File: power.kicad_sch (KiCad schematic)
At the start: 45 parts, among them U2 TPS56A37, U6 TPS5430DDA, U7 TPS56A37

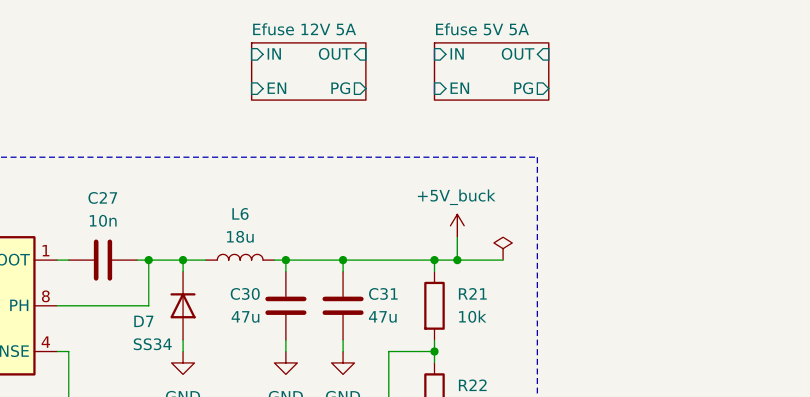
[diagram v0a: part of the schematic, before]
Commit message: schem: add ILM pins and 12V 10A rail
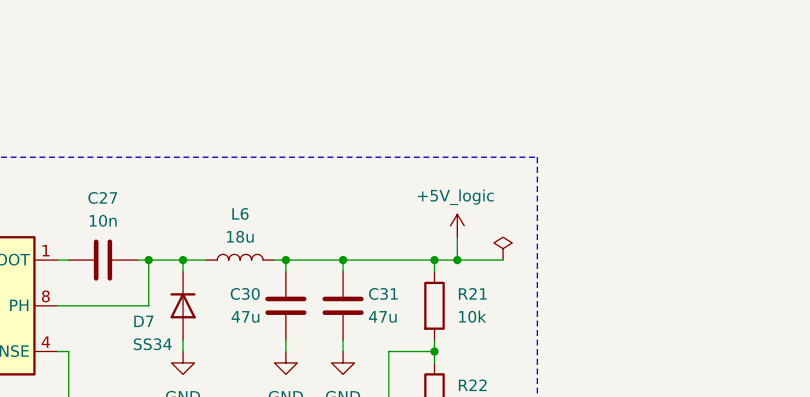
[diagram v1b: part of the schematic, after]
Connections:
- net +5V_buck renamed +5V_logic
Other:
- removed sheet Efuse 12V 5A
- removed sheet Efuse 5V 5A
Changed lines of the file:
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@@
 			)
 		)
-		(property "Value" "+5V_buck"
+		(property "Value" "+5V_logic"
 			(at 144.018 33.528 0)
 			(effects
@@
 				)
 			)
-		)
-	)
-	(sheet
-		(at 125.73 16.51)
-		(size 12.7 6.35)
-		(exclude_from_sim no)
-		(in_bom yes)
-		(on_board yes)
-		(dnp no)
-		(fields_autoplaced yes)
-		(stroke
-			(width 0.1524)
-			(type solid)
-		)
-		(fill
-			(color 0 0 0 0.0000)
-		)
-		(property "Sheetname" "Efuse 12V 5A"
-			(at 125.73 15.7984 0)
-			(effects
-				(font
-					(size 1.27 1.27)
-				)
-				(justify left bottom)
-			)
-		)
-		(property "Sheetfile" "efuse-12-5.kicad_sch"
-			(at 125.73 23.4446 0)
-			(effects
-				(font
-					(size 1.27 1.27)
-				)
-				(justify left top)
-				(hide yes)
-			)
-		)
-		(pin "EN" input
-			(at 125.73 21.59 180)
-			(effects
-				(font
-					(size 1.27 1.27)
-				)
-				(justify left)
-			)
-		)
-		(pin "PG" output
-			(at 138.43 21.59 0)
-			(effects
-				(font
-					(size 1.27 1.27)
-				)
-				(justify right)
-			)
-		)
-		(pin "OUT" input
-			(at 138.43 17.78 0)
-			(effects
-				(font
-					(size 1.27 1.27)
-				)
-				(justify right)
-			)
-		)
-		(pin "IN" input
-			(at 125.73 17.78 180)
-			(effects
-				(font
-					(size 1.27 1.27)
-				)
-				(justify left)
-			)
-		)
-		(instances
-			(project "valrob-carte-alim-cdf-1"
-				(path "/8d7b287d-627f-46aa-8c27-0b5ed29ab4a2/0cc01053-a223-4e8e-b0aa-a1ec618db290"
-					(page "3")
-				)
-			)
-		)
-	)
-	(sheet
-		(at 146.05 16.51)
-		(size 12.7 6.35)
-		(exclude_from_sim no)
-		(in_bom yes)
-		(on_board yes)
-		(dnp no)
-		(fields_autoplaced yes)
-		(stroke
-			(width 0.1524)
-			(type solid)
-		)
-		(fill
-			(color 0 0 0 0.0000)
-		)
-		(property "Sheetname" "Efuse 5V 5A"
-			(at 146.05 15.7984 0)
-			(effects
-				(font
-					(size 1.27 1.27)
-				)
-				(justify left bottom)
-			)
-		)
-		(property "Sheetfile" "efuse-5-5.kicad_sch"
-			(at 146.05 23.4446 0)
-			(effects
-				(font
-					(size 1.27 1.27)
-				)
-				(justify left top)
-				(hide yes)
-			)
-		)
-		(pin "EN" input
-			(at 146.05 21.59 180)
-			(effects
-				(font
-					(size 1.27 1.27)
-				)
-				(justify left)
-			)
-		)
-		(pin "PG" output
-			(at 158.75 21.59 0)
-			(effects
-				(font
-					(size 1.27 1.27)
-				)
-				(justify right)
-			)
-		)
-		(pin "OUT" input
-			(at 158.75 17.78 0)
-			(effects
-				(font
-					(size 1.27 1.27)
-				)
-				(justify right)
-			)
-		)
-		(pin "IN" input
-			(at 146.05 17.78 180)
-			(effects
-				(font
-					(size 1.27 1.27)
-				)
-				(justify left)
-			)
-		)
-		(instances
-			(project "valrob-carte-alim-cdf-1"
-				(path "/8d7b287d-627f-46aa-8c27-0b5ed29ab4a2/0cc01053-a223-4e8e-b0aa-a1ec618db290"
-					(page "4")
-				)
-			)

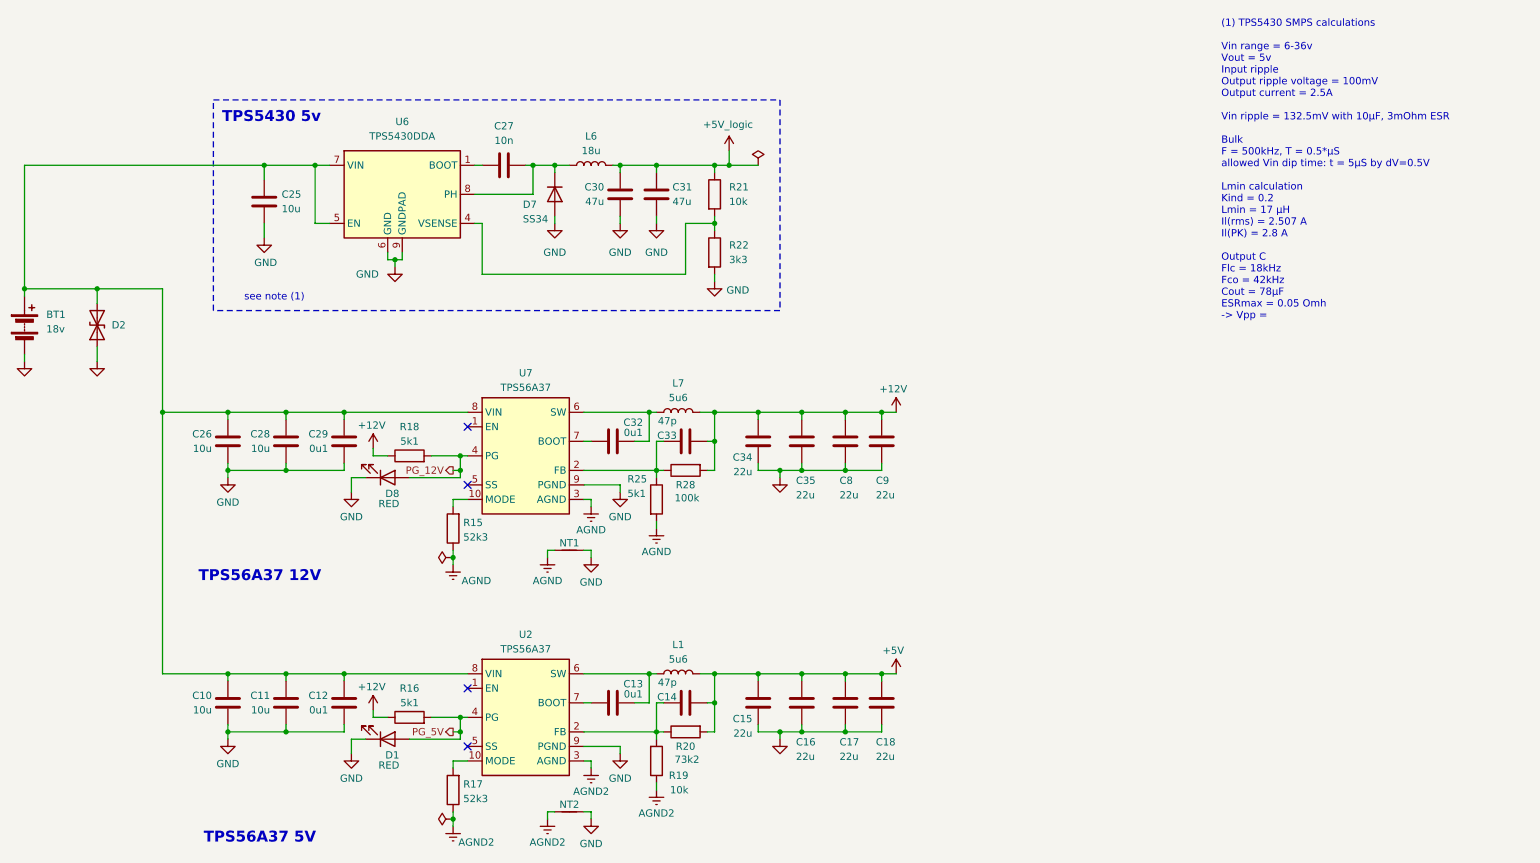
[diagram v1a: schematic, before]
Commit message: schem: reorganize connectors
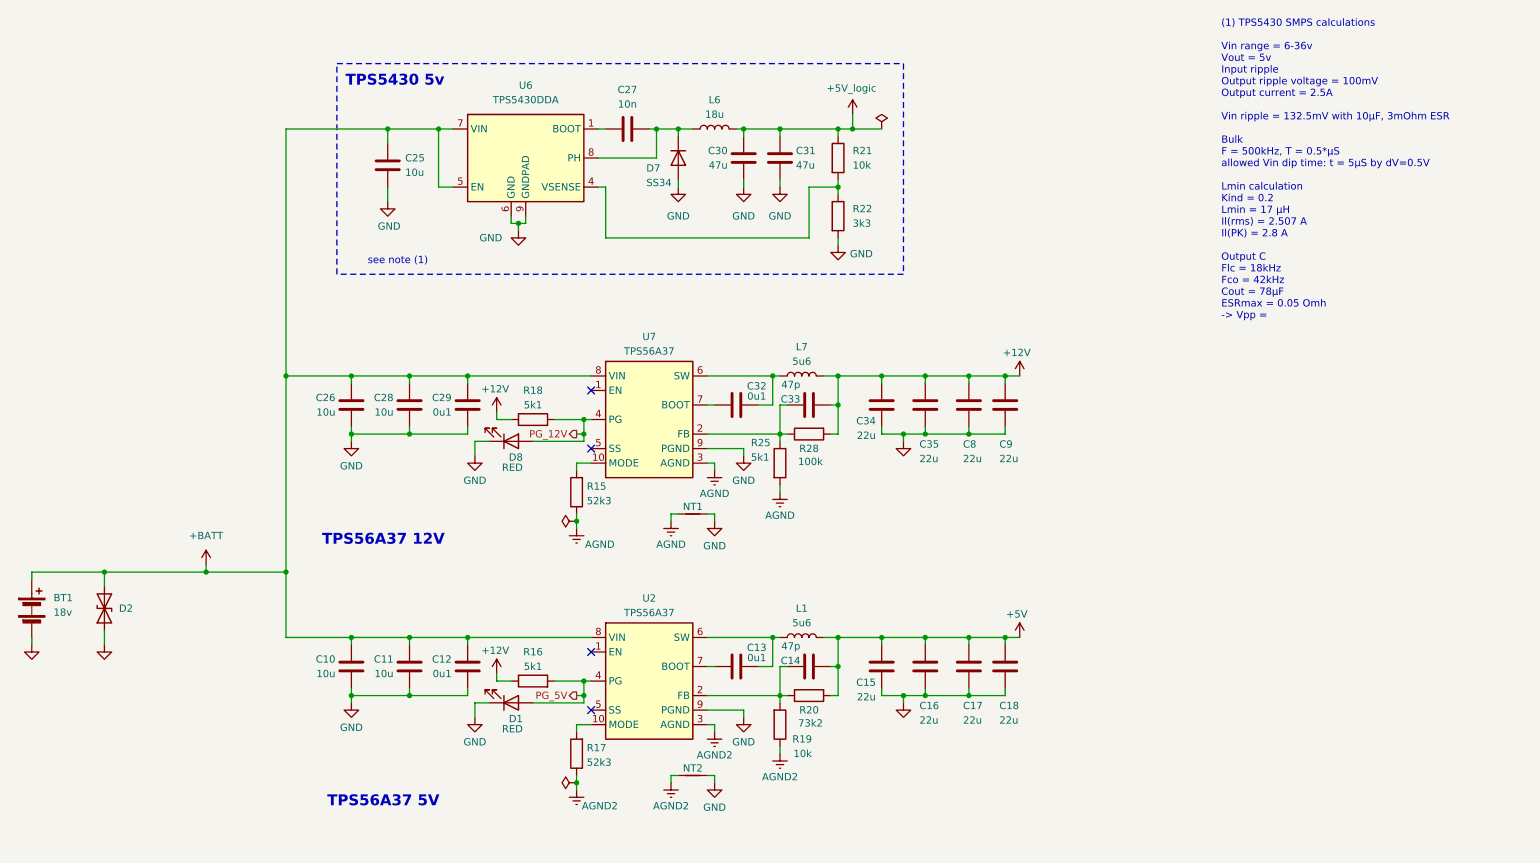
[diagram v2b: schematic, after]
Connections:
- net +BATT: now reaches BT1.1 (+), C10.1, C11.1, C12.1, C25.1, C26.1, C28.1, C29.1, D2.2 (A2), U2.8 (VIN), U6.5 (EN), U6.7 (VIN), U7.8 (VIN)
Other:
- moved on the sheet: BT1, C10, C11, C12, C13, C14, C15, C16, C17, C18, C25, C26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

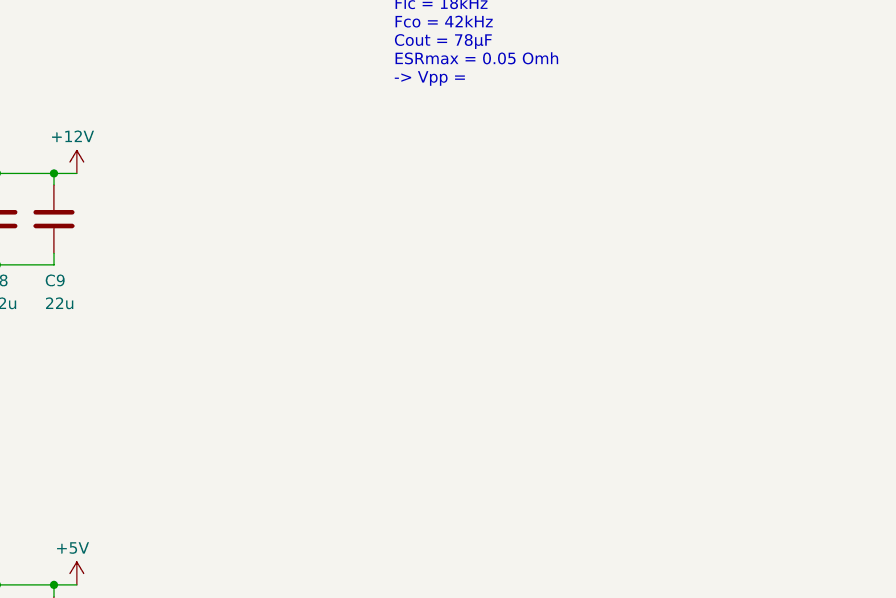
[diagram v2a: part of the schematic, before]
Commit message: schem: add CAN transceiver
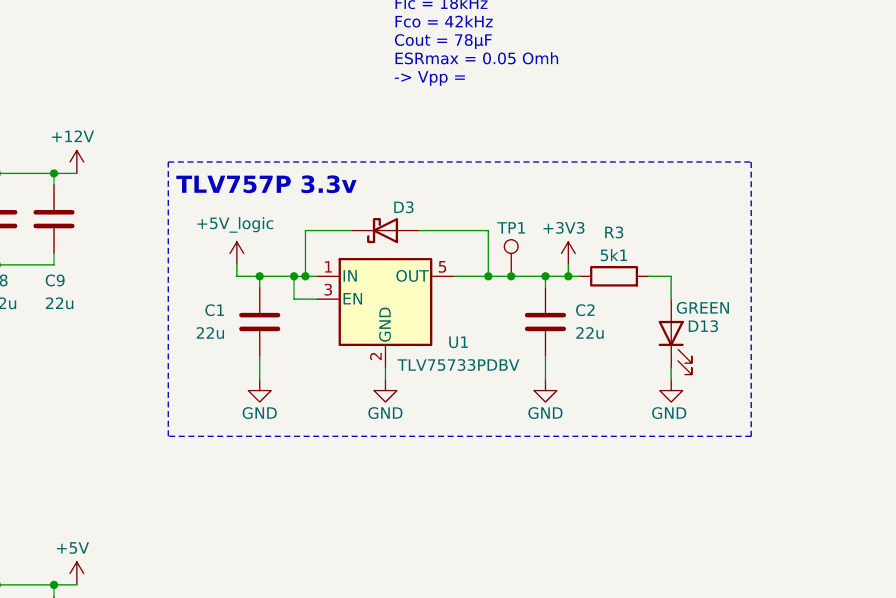
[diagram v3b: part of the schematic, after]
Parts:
- added C1, C2: 22u, Capacitor_SMD:C_0603_1608Metric, symbol Device:C
- added D13: GREEN, LED_SMD:LED_0805_2012Metric, symbol Device:LED
- added D3: D_Schottky, Diode_SMD:D_SMA, symbol Device:D_Schottky
- added R3: 5k1, Resistor_SMD:R_0402_1005Metric, symbol Device:R
- added TP1: TestPoint, TestPoint:TestPoint_Pad_D2.0mm, symbol Connector:TestPoint
- added U1: TLV75733PDBV, Package_TO_SOT_SMD:SOT-23-5, symbol Regulator_Linear:TLV75733PDBV
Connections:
- net +5V_logic: now also C1.2, D3.1 (K), U1.1 (IN), U1.3 (EN)
- net GND: now also C1.1, C2.1, D13.1 (K), U1.2 (GND)
- new net: D13.2 (A), R3.2
- new net +3V3: C2.2, D3.2 (A), R3.1, TP1.1, U1.5 (OUT)
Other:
- note added: "TLV757P 3.3v"

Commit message: schem: add additional connector for batt vin
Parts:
- added J25: Conn_01x02, Connector_JST:JST_XH_B2B-XH-A_1x02_P2.50mm_Vertical, symbol Connector_Generic:Conn_01x02
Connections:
- net +BATT: now also J25.2 (Pin_2)
- net GND: now also J25.1 (Pin_1)
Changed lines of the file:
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@@
 	)
 	(junction
+		(at 48.26 111.76)
+		(diameter 0)
+		(color 0 0 0 0)
+	)
+	(junction
 		(at 123.19 87.63)
 		(diameter 0)
@@
 	(wire
 		(pts
+			(xy 48.26 121.92) (xy 50.8 121.92)
+		)
+		(stroke
+			(width 0)
+			(type default)
+		)
+	)
+	(wire
+		(pts
 			(xy 127 53.34) (xy 127 44.45)
 		)
@@
 	(wire
 		(pts
-			(xy 39.37 111.76) (xy 57.15 111.76)
+			(xy 39.37 111.76) (xy 48.26 111.76)
 		)
 		(stroke
@@
 	(wire
 		(pts
+			(xy 48.26 119.38) (xy 48.26 111.76)
+		)
+		(stroke
+			(width 0)
+			(type default)
+		)
+	)
+	(wire
+		(pts
 			(xy 102.87 77.47) (xy 124.46 77.47)
 		)
@@
 	(wire
 		(pts
+			(xy 48.26 121.92) (xy 48.26 125.73)
+		)
+		(stroke
+			(width 0)
+			(type default)
+		)
+	)
+	(wire
+		(pts
 			(xy 190.5 133.35) (xy 196.85 133.35)
 		)
@@
 	(wire
 		(pts
+			(xy 50.8 119.38) (xy 48.26 119.38)
+		)
+		(stroke
+			(width 0)
+			(type default)
+		)
+	)
+	(wire
+		(pts
 			(xy 251.46 88.9) (xy 251.46 90.17)
 		)
@@
 	(wire
 		(pts
+			(xy 48.26 111.76) (xy 57.15 111.76)
+		)
+		(stroke
+			(width 0)
+			(type default)
+		)
+	)
+	(wire
+		(pts
 			(xy 151.13 90.17) (xy 144.78 90.17)
 		)
@@
 	)
 	(symbol
+		(lib_id "Connector_Generic:Conn_01x02")
+		(at 55.88 121.92 0)
+		(mirror x)
+		(unit 1)
+		(exclude_from_sim no)
+		(in_bom yes)
+		(on_board yes)
+		(dnp no)
+		(fields_autoplaced yes)
+		(property "Reference" "J25"
+			(at 55.88 115.57 0)
+			(effects
+				(font
+					(size 1.27 1.27)
+				)
+			)
+		)
+		(property "Value" "Conn_01x02"
+			(at 58.42 119.3801 0)
+			(effects
+				(font
+					(size 1.27 1.27)
+				)
+				(justify left)
+				(hide yes)
+			)
+		)
+		(property "Footprint" "Connector_JST:JST_XH_B2B-XH-A_1x02_P2.50mm_Vertical"
+			(at 55.88 121.92 0)
+			(effects
+				(font
+					(size 1.27 1.27)
+				)
+				(hide yes)
+			)
+		)
+		(property "Datasheet" "~"
+			(at 55.88 121.92 0)
+			(effects
+				(font
+					(size 1.27 1.27)
+				)
+				(hide yes)
+			)
+		)
+		(property "Description" "Generic connector, single row, 01x02, script generated (kicad-library-utils/schlib/autogen/connector/)"
+			(at 55.88 121.92 0)
+			(effects
+				(font
+					(size 1.27 1.27)
+				)
+				(hide yes)
+			)
+		)
+		(property "Basic" "Z"
+			(at 55.88 121.92 0)
+			(effects
+				(font
+					(size 1.27 1.27)
+				)
+				(hide yes)
+			)
+		)
+		(property "JLCPCB Part #" "C158012"
+			(at 55.88 121.92 0)
+			(effects
+				(font
+					(size 1.27 1.27)
+				)
+				(hide yes)
+			)
+		)
+		(property "Manufacturer" "JST"
+			(at 55.88 121.92 0)
+			(effects
+				(font
+					(size 1.27 1.27)
+				)
+				(hide yes)
+			)
+		)
+		(property "Manufacturer Part Number" "B2B-XH-A(LF)(SN)"
+			(at 55.88 121.92 0)
+			(effects
+				(font
+					(size 1.27 1.27)
+				)
+				(hide yes)
+			)
+		)
+		(pin "2"
+		)
+		(pin "1"
+		)
+		(instances
+			(project "valrob-carte-alim-cdf-1"
+				(path "/8d7b287d-627f-46aa-8c27-0b5ed29ab4a2/0cc01053-a223-4e8e-b0aa-a1ec618db290"
+					(reference "J25")
+					(unit 1)
+				)
+			)
+		)
+	)
+	(symbol
 		(lib_id "power:+12V")
 		(at 199.39 77.47 0)
@@
 					(unit 1)
 				)
+			)
+		)
+	)
+	(symbol
+		(lib_id "power:GND")
+		(at 48.26 125.73 0)
+		(unit 1)
+		(exclude_from_sim no)
+		(in_bom yes)
+		(on_board yes)
+		(dnp no)
+		(fields_autoplaced yes)
+		(property "Reference" "#PWR042"
+			(at 48.26 132.08 0)
+			(effects
+				(font
+					(size 1.27 1.27)
+				)
+				(hide yes)
+			)
+		)
+		(property "Value" "GND"
+			(at 48.26 130.81 0)
+			(effects
+				(font
+					(size 1.27 1.27)
+				)
+				(hide yes)
+			)
+		)
+		(property "Footprint" ""
+			(at 48.26 125.73 0)
+			(effects
+				(font
+					(size 1.27 1.27)
+				)
+				(hide yes)
+			)
+		)
+		(property "Datasheet" ""
+			(at 48.26 125.73 0)
+			(effects
+				(font
+					(size 1.27 1.27)
+				)
+				(hide yes)
+			)
+		)
+		(property "Description" "Power symbol creates a global label with name \"GND\" , ground"
+			(at 48.26 125.73 0)
+			(effects
+				(font
+					(size 1.27 1.27)
+				)
+				(hide yes)
+			)
+		)
+		(pin "1"
+		)
+		(instances
+			(project "valrob-carte-alim-cdf-1"
+				(path "/8d7b287d-627f-46aa-8c27-0b5ed29ab4a2/0cc01053-a223-4e8e-b0aa-a1ec618db290"
+					(reference "#PWR042")
+					(unit 1)
+				)
